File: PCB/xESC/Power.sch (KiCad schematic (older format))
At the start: 25 parts, among them U2 TMC6100-LA, U3 MCP601R

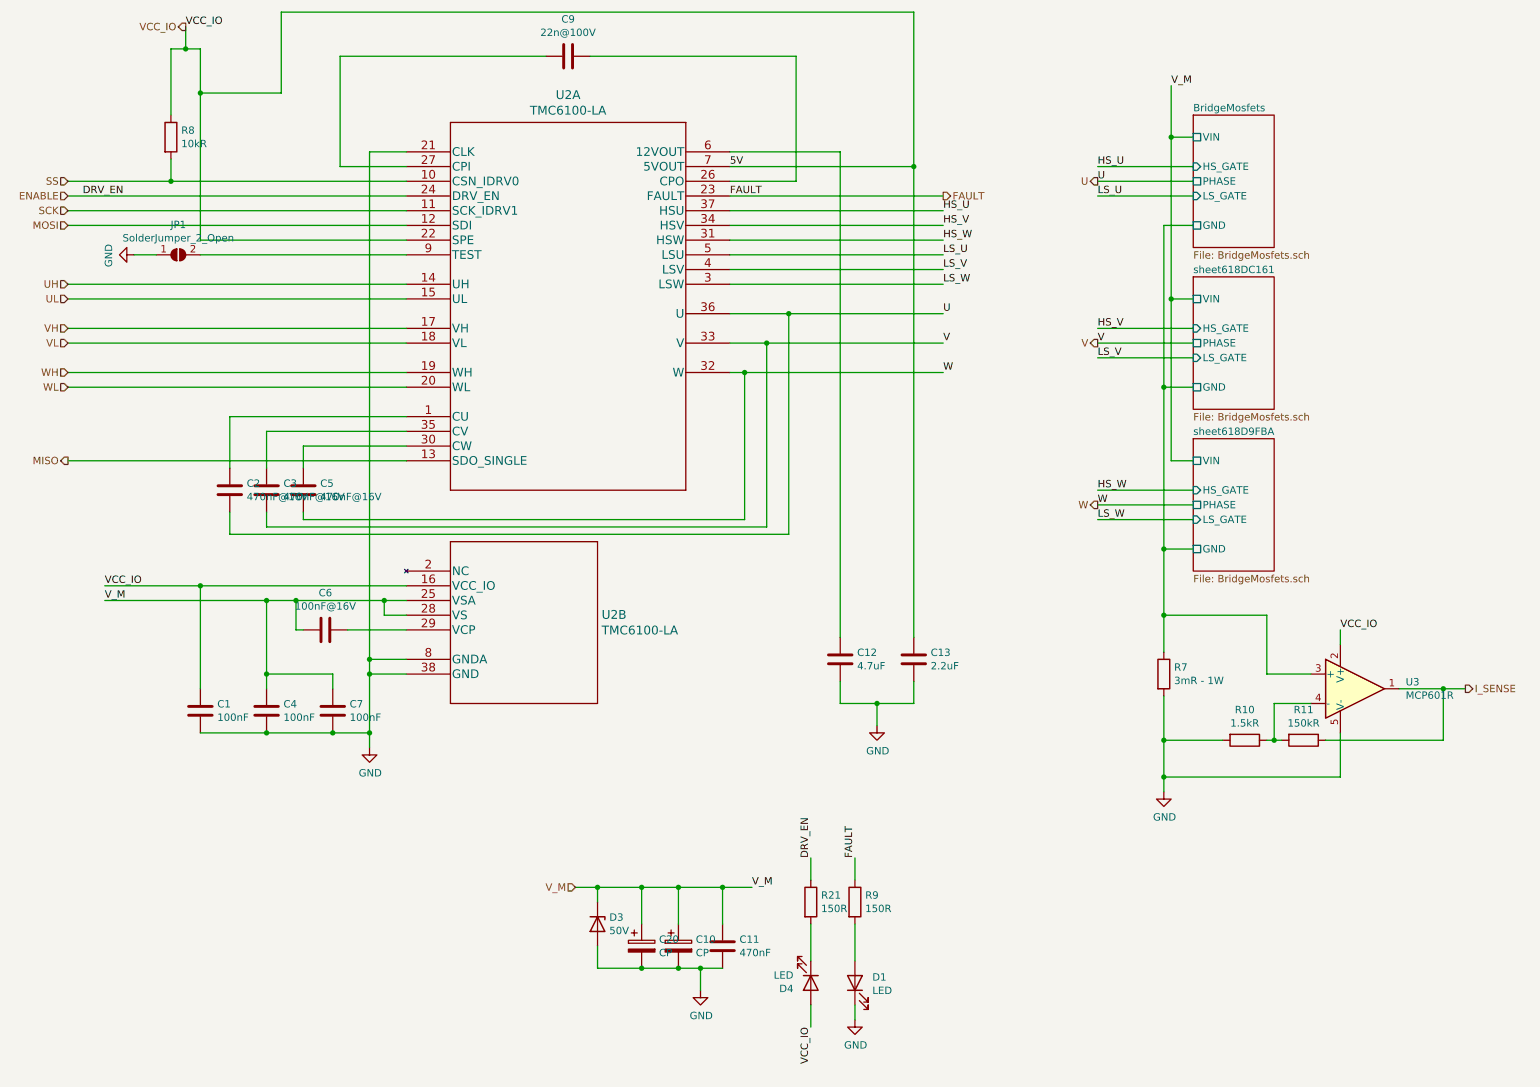
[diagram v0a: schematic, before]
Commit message: changed some values, added BOM
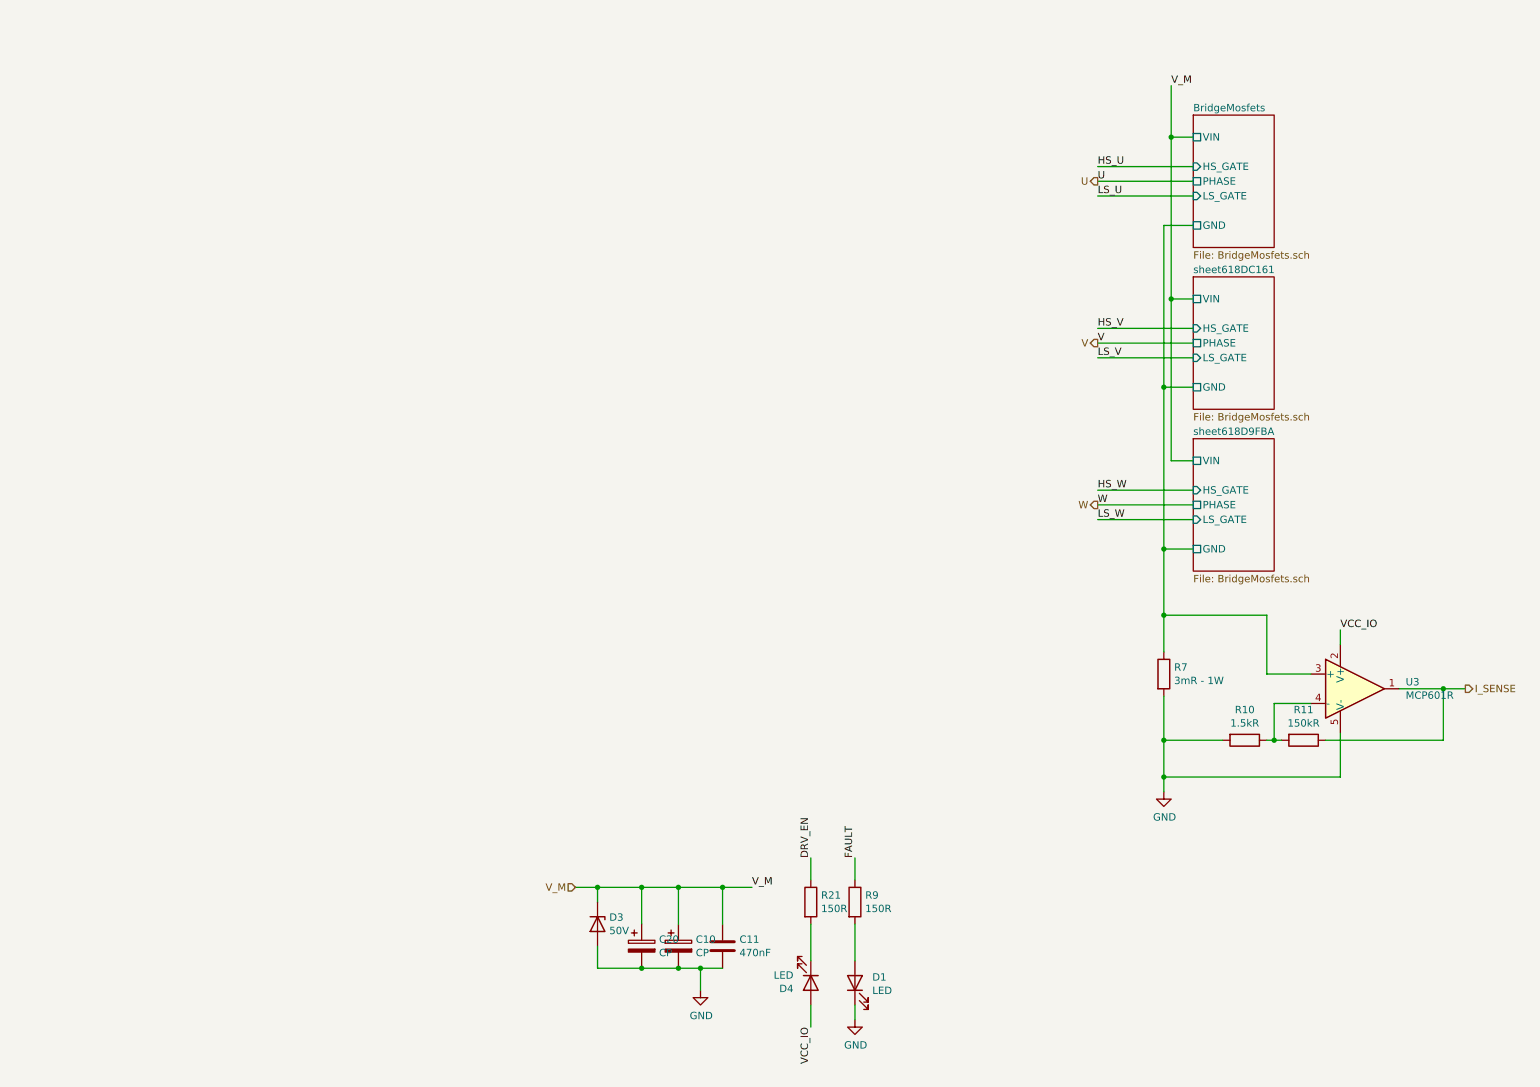
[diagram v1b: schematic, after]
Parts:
- removed C1, C4, C7: 100nF, Capacitor_SMD:C_0805_2012Metric_Pad1.18x1.45mm_HandSolder, symbol Device:C
- removed C12: 4.7uF, Capacitor_SMD:C_0805_2012Metric_Pad1.18x1.45mm_HandSolder, symbol Device:C
- removed C13: 2.2uF, Capacitor_SMD:C_0805_2012Metric_Pad1.18x1.45mm_HandSolder, symbol Device:C
- removed C2, C3, C5: 470nF@16V, Capacitor_SMD:C_0805_2012Metric_Pad1.18x1.45mm_HandSolder, symbol Device:C
- removed C6: 100nF@16V, Capacitor_SMD:C_0805_2012Metric_Pad1.18x1.45mm_HandSolder, symbol Device:C
- removed C9: 22n@100V, Capacitor_SMD:C_0805_2012Metric_Pad1.18x1.45mm_HandSolder, symbol Device:C
- removed JP1: SolderJumper_2_Open, Jumper:SolderJumper-2_P1.3mm_Open_Pad1.0x1.5mm, symbol Jumper:SolderJumper_2_Open
- removed R8: 10kR, Resistor_SMD:R_0805_2012Metric, symbol Device:R
- removed U2: TMC6100-LA, footprints:TMC6100-LA, symbol TMC6100:TMC6100-LA
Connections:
- net ENABLE renamed DRV_EN
